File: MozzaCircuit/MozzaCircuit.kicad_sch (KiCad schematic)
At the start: 104 parts, among them SW11 SW_ChocV2_rev, SW12 SW_ChocV2_rev, SW13 SW_ChocV2_rev, SW14 SW_ChocV2_rev, SW15 SW_ChocV2_rev, SW21 SW_ChocV2_rev

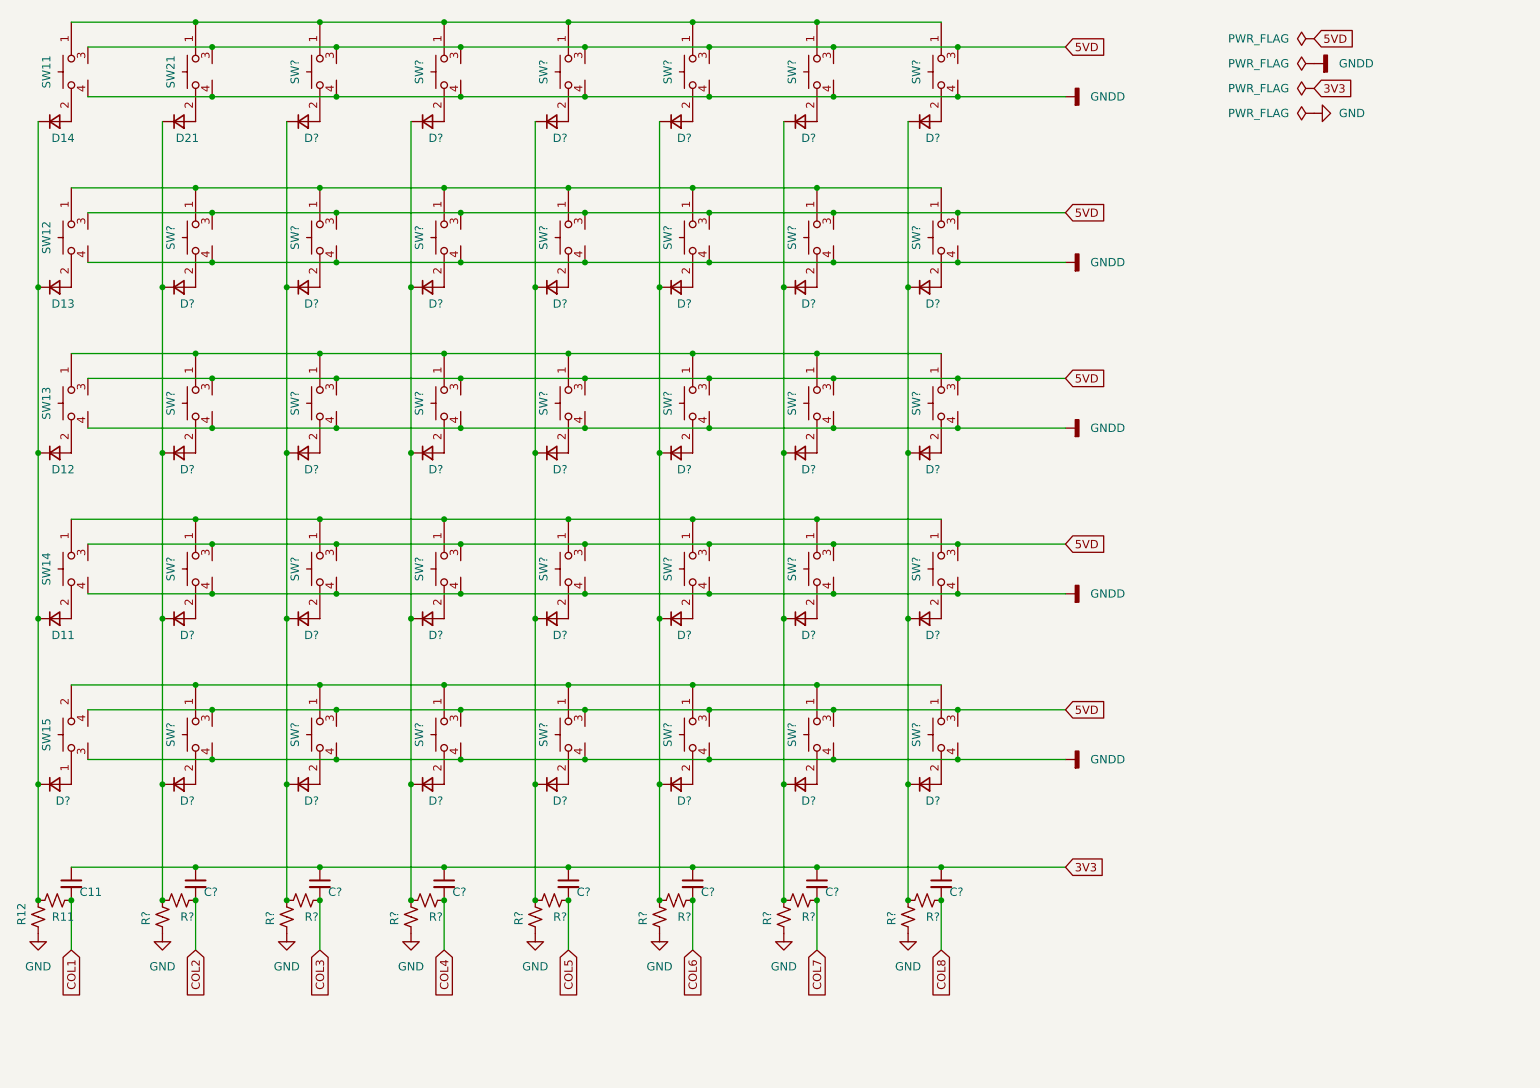
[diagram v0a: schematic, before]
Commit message: switch matrix
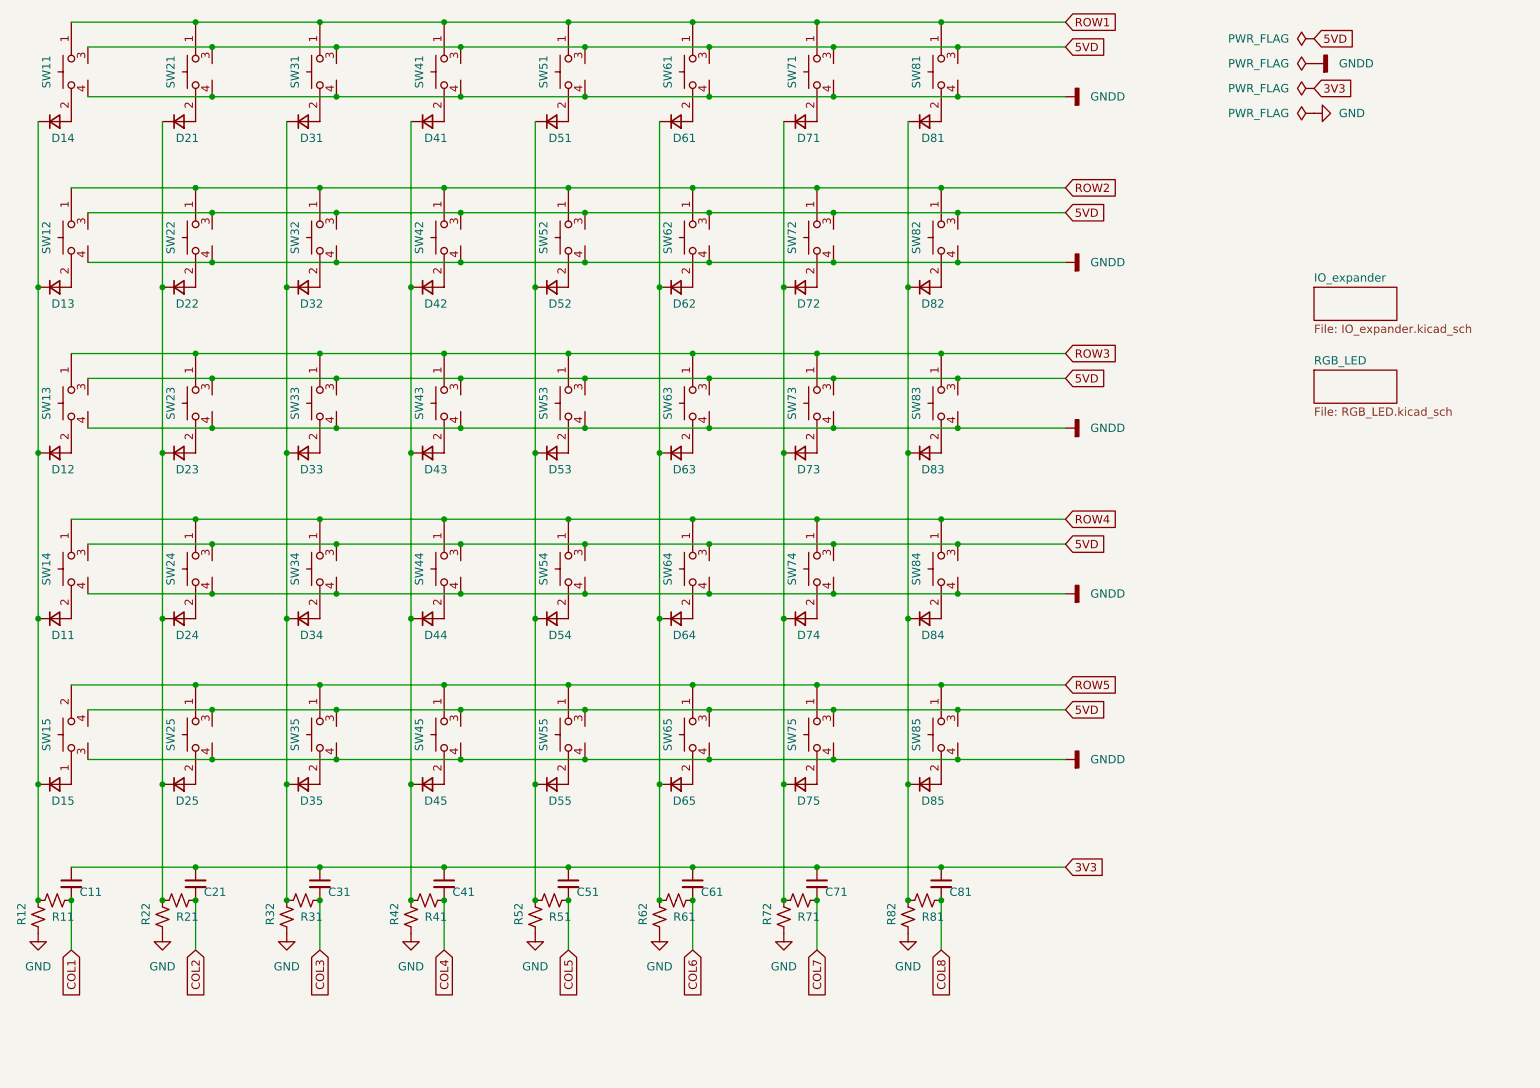
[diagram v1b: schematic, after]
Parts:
- gave numbers to parts that had none: 90
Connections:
- net ROW4: now reaches SW14.1, SW24.1, SW34.1, SW44.1, SW54.1, SW64.1, SW74.1, SW84.1
- net ROW5: now reaches SW15.2, SW25.1, SW35.1, SW45.1, SW55.1, SW65.1, SW75.1, SW85.1
- net ROW2: now reaches SW12.1, SW22.1, SW32.1, SW42.1, SW52.1, SW62.1, SW72.1, SW82.1
- net ROW3: now reaches SW13.1, SW23.1, SW33.1, SW43.1, SW53.1, SW63.1, SW73.1, SW83.1
- net ROW1: now reaches SW11.1, SW21.1, SW31.1, SW41.1, SW51.1, SW61.1, SW71.1, SW81.1
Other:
- added sheet IO_expander (IO_expander.kicad_sch)
- added sheet RGB_LED (RGB_LED.kicad_sch)

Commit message: added rotary encoder
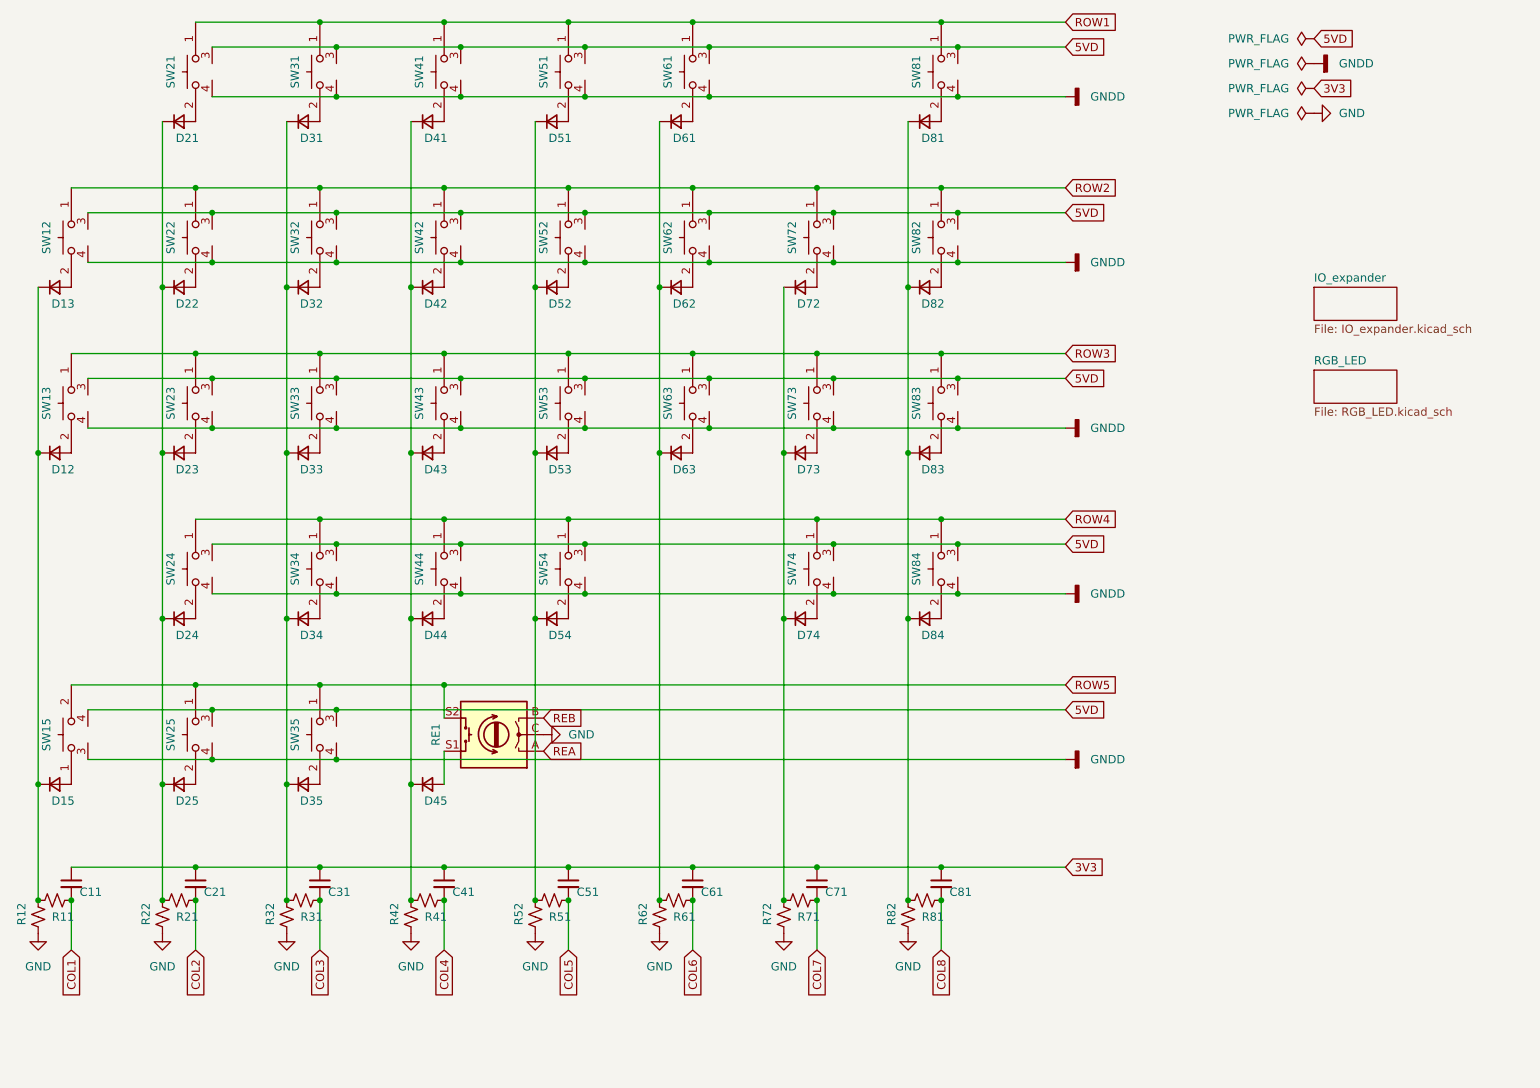
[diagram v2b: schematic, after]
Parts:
- removed D11, D14, D55, D64, D65, D71, D75, D85: D_Small, symbol Device:D_Small
- removed SW11, SW14, SW45, SW55, SW64, SW65, SW71, SW75, SW85: SW_ChocV2_rev, symbol 00_KeyParts:SW_ChocV2_rev
- added RE1: RotaryEncoder_Switch, symbol Device:RotaryEncoder_Switch
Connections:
- net GND: now also RE1.C
- net ROW5: now also RE1.S2
- net at D45.2 (A): now also RE1.S1
- new net REA: RE1.A
- new net REB: RE1.B

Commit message: led matrix
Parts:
- removed C11, C21, C31, C41, C51, C61, C71, C81: C_Small, symbol Device:C_Small
- removed D12, D13, D15, D21, D22, D23, D24, D25, D31, D32, D33, D34, D35, D41, D42, D43, D44, D45, D51, D52, D53, D54, D61, D62, D63, D72, D73, D74, D81, D82, D83, D84: D_Small, symbol Device:D_Small
- removed R11, R12, R21, R22, R31, R32, R41, R42, R51, R52, R61, R62, R71, R72, R81, R82: R_Small_US, symbol Device:R_Small_US
- removed RE1: RotaryEncoder_Switch, symbol Device:RotaryEncoder_Switch
- removed SW12, SW13, SW15, SW21, SW22, SW23, SW24, SW25, SW31, SW32, SW33, SW34, SW35, SW41, SW42, SW43, SW44, SW51, SW52, SW53, SW54, SW61, SW62, SW63, SW72, SW73, SW74, SW81, SW82, SW83, SW84: SW_ChocV2_rev, symbol 00_KeyParts:SW_ChocV2_rev
- added C1, C2: C_Small, symbol Device:C_Small
- added J1: 8P8C_both_sides, symbol 00_KeyParts:8P8C_both_sides
- added JPB2, JPB3, JPB4, JPB6, JPB7, JPB8, JPF2, JPF3, JPF4, JPF6, JPF7, JPF8: SolderJumper_2_Open, symbol Jumper:SolderJumper_2_Open
- added U1, U2: MCP23017_ML, Package_DFN_QFN:QFN-28-1EP_6x6mm_P0.65mm_EP4.25x4.25mm, symbol Interface_Expansion:MCP23017_ML
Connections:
- net 3V3: now also C1.1, C2.1, JPB3.2 (B), JPF3.2 (B), U1.5 (VDD), U2.11 (A0), U2.5 (VDD)
- net 5VD: now also J1.5
- net COL1: now also U1.17 (GPA0), U2.17 (GPA0)
- net COL2: now also U1.18 (GPA1), U2.18 (GPA1)
- net COL3: now also U1.19 (GPA2), U2.19 (GPA2)
- net COL4: now also U1.20 (GPA3), U2.20 (GPA3)
- net COL5: now also U1.21 (GPA4), U2.21 (GPA4)
- net COL6: now also U1.22 (GPA5), U2.22 (GPA5)
- net COL7: now also U1.23 (GPA6), U2.23 (GPA6)
- net COL8: now also U1.24 (GPA7), U2.24 (GPA7)
- net GND: now also C1.2, C2.2, JPB2.2 (B), JPF2.2 (B), U1.11 (A0), U1.12 (A1), U1.13 (A2), U1.29 (EP), U1.6 (VSS), U2.12 (A1), U2.13 (A2), U2.29 (EP), U2.6 (VSS)
- net GNDD: now also JPB4.2 (B), JPF4.2 (B)
- net REA: now also U1.2 (GPB5), U2.2 (GPB5)
- net REB: now also U1.3 (GPB6), U2.3 (GPB6)
- net ROW1: now also U1.25 (GPB0), U2.25 (GPB0)
- net ROW2: now also U1.26 (GPB1), U2.26 (GPB1)
- net ROW3: now also U1.27 (GPB2), U2.27 (GPB2)
- net ROW4: now also U1.28 (GPB3), U2.28 (GPB3)
- net ROW5: now also U1.1 (GPB4), U2.1 (GPB4)
- new net: J1.7 (3), JPB3.1 (A), JPF7.1 (A)
- new net: J1.3 (7), JPB7.1 (A), JPF3.1 (A)
- new net: J1.2 (8), JPB8.1 (A), JPF2.1 (A)
- new net: J1.8 (2), JPB2.1 (A), JPF8.1 (A)
- new net: J1.6 (4), JPB4.1 (A), JPF6.1 (A)
- new net: J1.4 (6), JPB6.1 (A), JPF4.1 (A)
- new net LED: J1.1, J1.9 (1)
- new net NRST: JPB6.2 (B), JPF6.2 (B), U1.14 (~{RESET}), U2.14 (~{RESET})
- new net SCK: JPB7.2 (B), JPF7.2 (B), U1.8 (SCK), U2.8 (SCK)
- new net SDA: JPB8.2 (B), JPF8.2 (B), U1.9 (SDA), U2.9 (SDA)
- no-connect marks 0 -> 6
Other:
- removed sheet IO_expander
- added sheet SwitchMatrix (SwitchMatrix.kicad_sch)

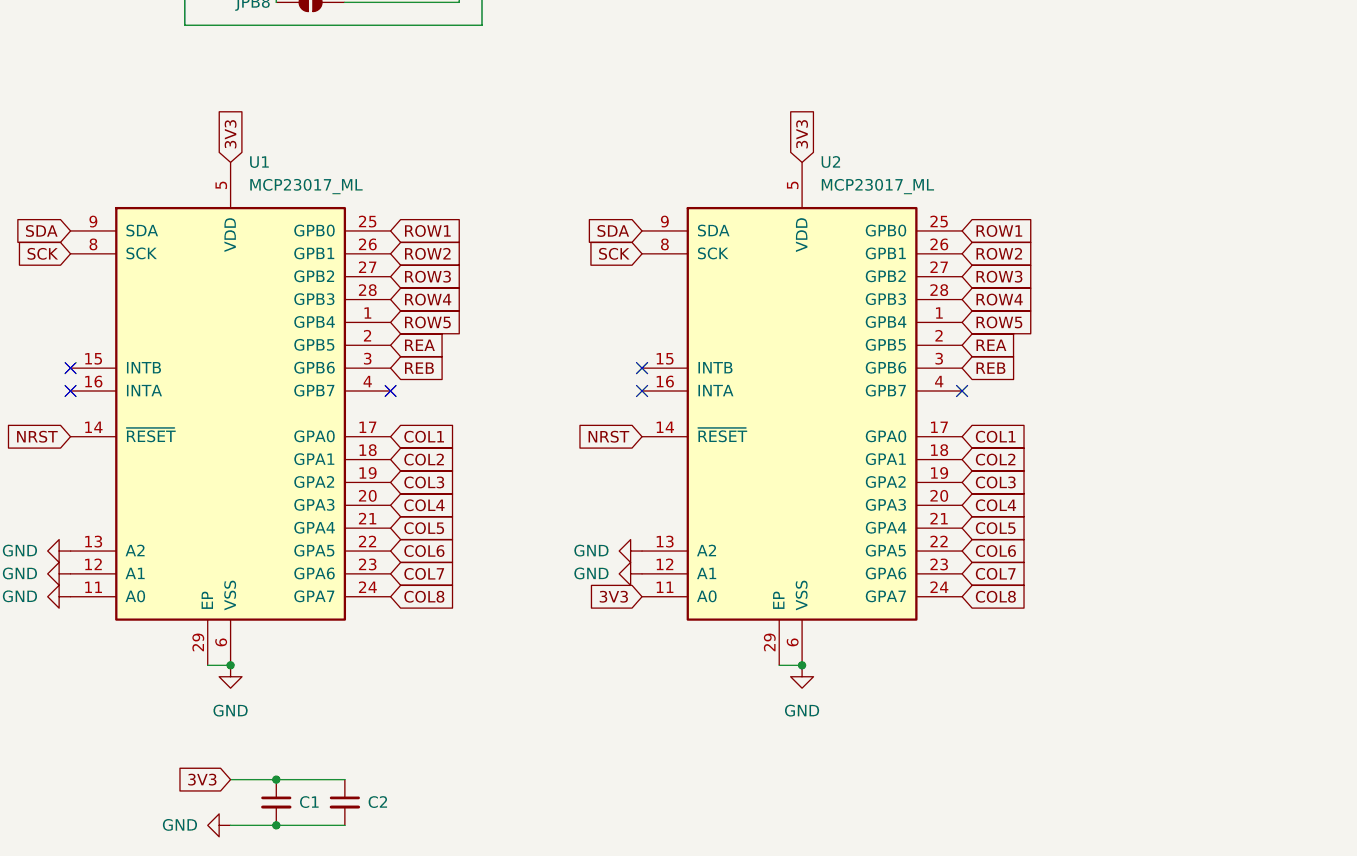
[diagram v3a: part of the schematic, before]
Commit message: added 3D models, debounce for encoder
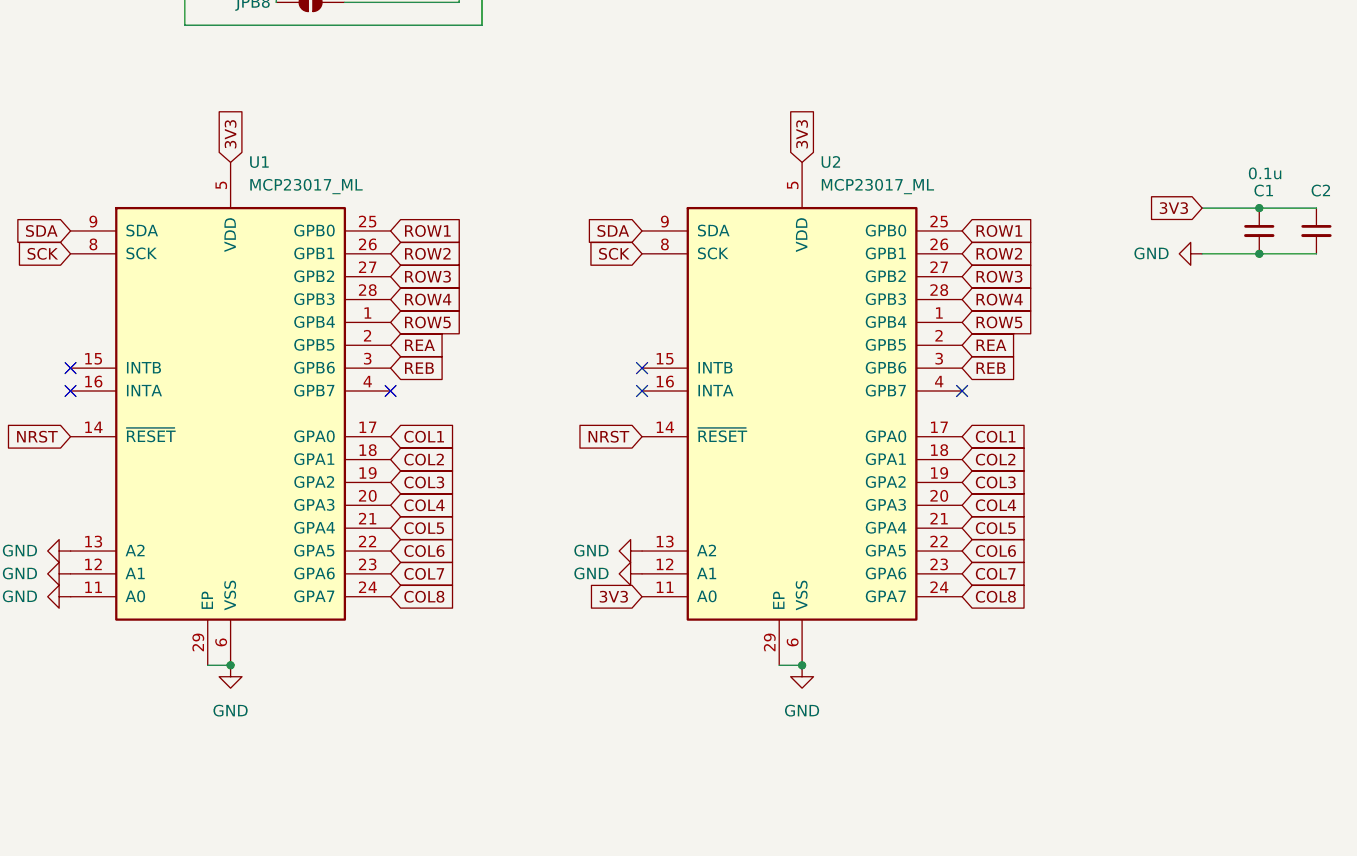
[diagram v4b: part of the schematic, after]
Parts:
- C1: value C_Small -> 0.1u; footprint (none) -> 00_KeyParts:C_2012
- C2: footprint (none) -> 00_KeyParts:C_2012
- J1: footprint (none) -> 00_KeyParts:RJ45_Molex_0955032884_both_sides
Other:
- moved on the sheet: C1, C2

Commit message: added qfn footprints
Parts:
- U1: footprint Package_DFN_QFN:QFN-28-1EP_6x6mm_P0.65mm_EP4.25x4.25mm -> 00_KeyParts:QFN-28-1EP_6x6mm_P0.65mm_EP4.25x4.25mm_Hand
- U2: footprint Package_DFN_QFN:QFN-28-1EP_6x6mm_P0.65mm_EP4.25x4.25mm -> 00_KeyParts:QFN-28-1EP_6x6mm_P0.65mm_EP4.25x4.25mm_Hand_NoTP
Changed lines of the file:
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@@
       (effects (font (size 1.27 1.27)) (justify left))
     )
-    (property "Footprint" "Package_DFN_QFN:QFN-28-1EP_6x6mm_P0.65mm_EP4.25x4.25mm" (id 2) (at 119.38 162.56 0)
+    (property "Footprint" "00_KeyParts:QFN-28-1EP_6x6mm_P0.65mm_EP4.25x4.25mm_Hand_NoTP" (id 2) (at 119.38 162.56 0)
       (effects (font (size 1.27 1.27)) (justify left) hide)
     )
@@
       (effects (font (size 1.27 1.27)) (justify left))
     )
-    (property "Footprint" "Package_DFN_QFN:QFN-28-1EP_6x6mm_P0.65mm_EP4.25x4.25mm" (id 2) (at 55.88 162.56 0)
+    (property "Footprint" "00_KeyParts:QFN-28-1EP_6x6mm_P0.65mm_EP4.25x4.25mm_Hand" (id 2) (at 55.88 162.56 0)
       (effects (font (size 1.27 1.27)) (justify left) hide)
     )
@@
       (reference "#PWR0121") (unit 1) (value "GND") (footprint "")
     )
+    (path "/640a3fc7-fa1f-4829-bcbd-ff561d335477/aea38b8b-e93d-472f-9cc7-986e6b10611f"
+      (reference "#PWR0122") (unit 1) (value "GND") (footprint "")
+    )
     (path "/640a3fc7-fa1f-4829-bcbd-ff561d335477/5752b83b-3c53-4389-b95f-3cdceafd04b6"
       (reference "#PWR0123") (unit 1) (value "GNDD") (footprint "")
@@
     )
     (path "/640a3fc7-fa1f-4829-bcbd-ff561d335477/32702db2-55bb-4fdc-abdb-b8636689ac2e"
-      (reference "#PWR?") (unit 1) (value "GND") (footprint "")
-    )
-    (path "/640a3fc7-fa1f-4829-bcbd-ff561d335477/aea38b8b-e93d-472f-9cc7-986e6b10611f"
-      (reference "#PWR?") (unit 1) (value "GND") (footprint "")
+      (reference "#PWR0137") (unit 1) (value "GND") (footprint "")
     )
     (path "/0cdca463-f442-4a42-be31-f71e125b5c6a"
@@
       (reference "C84") (unit 1) (value "C_Small") (footprint "00_KeyParts:C_2012_rev")
     )
+    (path "/640a3fc7-fa1f-4829-bcbd-ff561d335477/481ff183-85e3-4c7e-9a5b-1988a8ca38ab"
+      (reference "CA1") (unit 1) (value "33n") (footprint "00_KeyParts:C_2012_rev")
+    )
+    (path "/640a3fc7-fa1f-4829-bcbd-ff561d335477/bdb40568-967c-4768-8565-b012d5df3e69"
+      (reference "CB1") (unit 1) (value "C_Small") (footprint "00_KeyParts:C_2012_rev")
+    )
     (path "/640a3fc7-fa1f-4829-bcbd-ff561d335477/f4b8ad53-f2ef-41a9-becd-fa8a5cce0915"
       (reference "CD1") (unit 1) (value "33n") (footprint "00_KeyParts:C_2012_rev")
@@
       (reference "CD8") (unit 1) (value "C_Small") (footprint "00_KeyParts:C_2012_rev")
     )
-    (path "/640a3fc7-fa1f-4829-bcbd-ff561d335477/481ff183-85e3-4c7e-9a5b-1988a8ca38ab"
-      (reference "CDA") (unit 1) (value "33n") (footprint "00_KeyParts:C_2012_rev")
-    )
-    (path "/640a3fc7-fa1f-4829-bcbd-ff561d335477/bdb40568-967c-4768-8565-b012d5df3e69"
-      (reference "CDB") (unit 1) (value "C_Small") (footprint "00_KeyParts:C_2012_rev")
-    )
     (path "/640a3fc7-fa1f-4829-bcbd-ff561d335477/991c063e-ad48-4121-ada9-51d9b41237fa"
       (reference "D12") (unit 1) (value "D_Small") (footprint "00_KeyParts:D_SOD-323_both_sides")
@@
     )
     (path "/26b4e507-cb67-46fc-a000-dfe1a1a16591"
-      (reference "U1") (unit 1) (value "MCP23017_ML") (footprint "Package_DFN_QFN:QFN-28-1EP_6x6mm_P0.65mm_EP4.25x4.25mm")
+      (reference "U1") (unit 1) (value "MCP23017_ML") (footprint "00_KeyParts:QFN-28-1EP_6x6mm_P0.65mm_EP4.25x4.25mm_Hand")
     )
     (path "/21c35884-09fe-4da8-a010-f2b680d013b0"
-      (reference "U2") (unit 1) (value "MCP23017_ML") (footprint "Package_DFN_QFN:QFN-28-1EP_6x6mm_P0.65mm_EP4.25x4.25mm")
-    )
-  )
+      (reference "U2") (unit 1) (value "MCP23017_ML") (footprint "00_KeyParts:QFN-28-1EP_6x6mm_P0.65mm_EP4.25x4.25mm_Hand_NoTP")
+    )
+  )
